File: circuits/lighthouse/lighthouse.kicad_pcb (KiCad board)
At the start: 2 copper layers, 83 x 80 mm, 96 parts, among them IC1 SX1308, J1 USB_C_Receptacle_USB2.0_14P, J2 Conn_01x03_Socket, Q1 S9013, Q2 FS8205A, Q3 2N7002K, Q4 SS8050, Q5 SS8050, U1 R300, U10 CP2102-GMR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

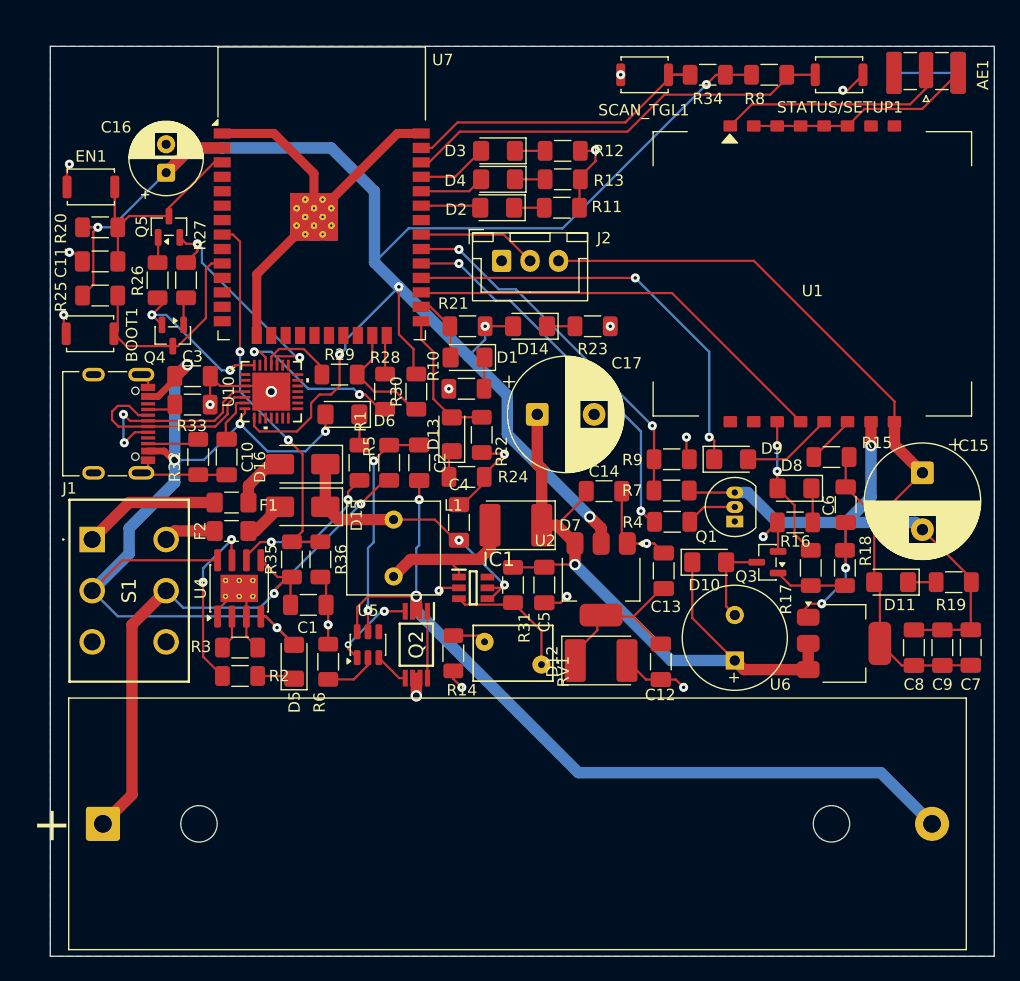
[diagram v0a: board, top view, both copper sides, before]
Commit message: Removed silkscreen numbering
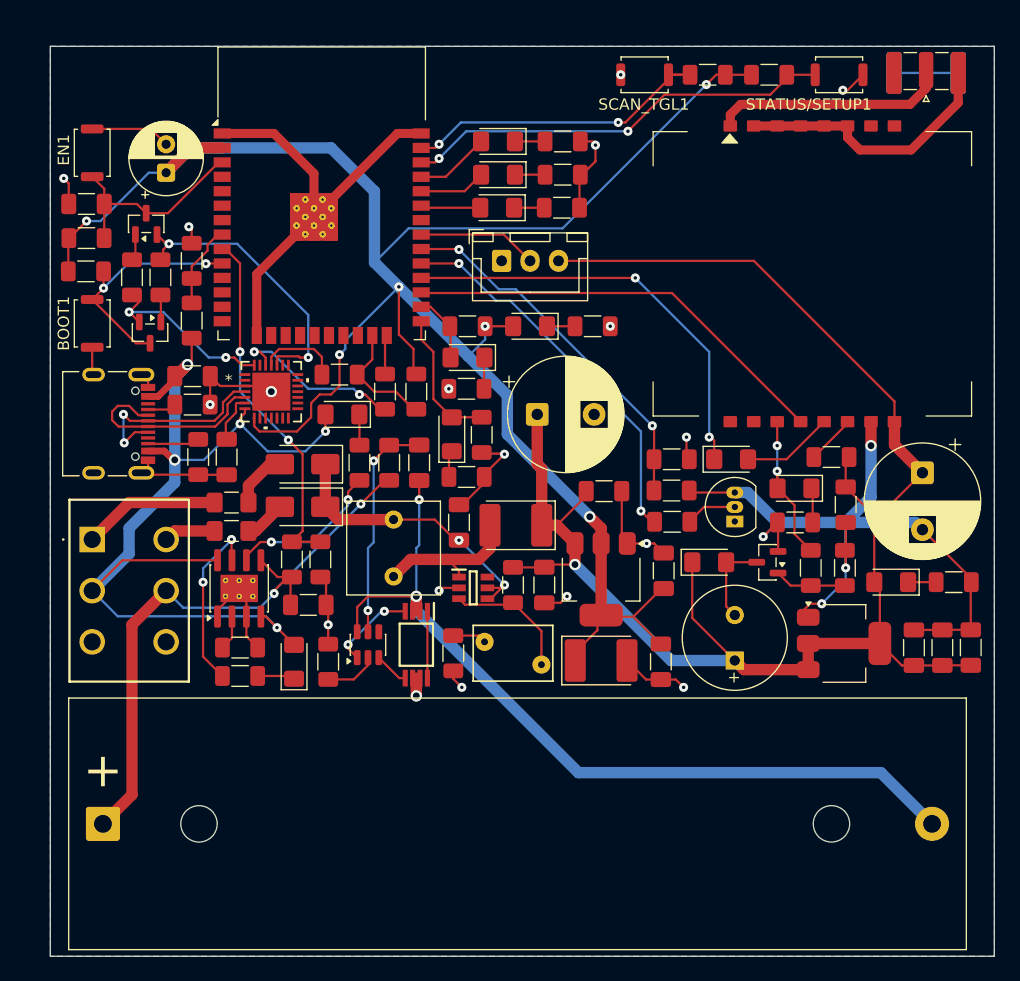
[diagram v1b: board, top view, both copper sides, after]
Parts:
- added R37: 47k, Resistor_SMD:R_1206_3216Metric_Pad1.30x1.75mm_HandSolder, F.Cu at (44.5, 73.2)
- added R38: 100k, Resistor_SMD:R_1206_3216Metric_Pad1.30x1.75mm_HandSolder, F.Cu at (44.5, 78.5)
- moved C11 5.19 mm to (35.2, 68.2)
- moved EN1 3.00 mm to (35.8, 63.8), turned to -90 degrees
- moved R25 2.46 mm to (35.2, 74.2)
- moved R26 2.26 mm to (39.2, 74.7)
- moved R27 2.26 mm to (41.8, 74.7)
- moved Q4 2.02 mm to (40.8, 79.6)
- moved Q5 2.02 mm to (40.5, 70.0)
- moved R20 1.53 mm to (35.2, 71.2)
- moved BOOT1 0.93 mm to (35.8, 78.8), turned to 90 degrees
- moved D3 0.83 mm to (71.4, 62.8)
- moved R12 0.83 mm to (77.1, 62.8)
- moved D4 0.41 mm to (71.4, 65.7)
- moved R13 0.41 mm to (77.1, 65.7)
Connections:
- U7 pad 8: ADS_BAT -> USB_SENSE
- U7 pad 9: unconnected-(U7-IO33-Pad9) -> ADS_BAT
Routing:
- net GND: track 123.4 -> 131.6 mm, vias 19 -> 18
- net USB_SENSE: track 0.00 -> 7.35 mm
- net +5V: track 135.6 -> 141.9 mm
- net MP24: track 20.5 -> 25.1 mm
- net +3.3V: track 171.2 -> 175.5 mm
- net Net-(AE1-Shield): track 25.8 -> 29.7 mm
- net ESP25: track 19.1 -> 21.0 mm, vias 0 -> 2
- net MP28: track 13.9 -> 15.6 mm
- net ADS_BAT: track 33.6 -> 32.0 mm
- net Net-(U7-IO22): track 37.4 -> 38.2 mm, vias 0 -> 2
- net Net-(Q4-B): track 3.12 -> 2.46 mm
- net Net-(AE1-A): track 20.2 -> 20.8 mm
- net Net-(U10-RXD): track 6.79 -> 7.32 mm
- net Net-(U7-IO23): vias 0 -> 2
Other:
- board text removed: "R9"

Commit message: Safekeeping
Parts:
- removed R31: 1k, Resistor_SMD:R_1206_3216Metric_Pad1.30x1.75mm_HandSolder
- removed S1: SLW-1678105-6A-N-D, SLW-1678105-6A-N-D:SLW16781056AND
- added SW1: SW_Push_DPDT, Connector_JST:JST_XH_B4B-XH-A_1x04_P2.50mm_Vertical, F.Cu at (38.2, 105.5)
- D1, D2, D3, D4: footprint LED_SMD:LED_1206_3216Metric_Pad1.42x1.75mm_HandSolder -> LED_THT:LED_D3.0mm
- Q1: value S9013 -> BC337
- Q4, Q5: value SS8050 -> BC817-40
- R14: value 200 -> 220
- R4: value 240 -> 150
- R7: value 10k -> 100k
- R9: value 20k -> 47k
- RV1: value 8k4 -> W103; footprint Varistor:RV_Disc_D7mm_W4.9mm_P5mm -> 3296W-1-103LF:3296W1503LF
- moved R14 8.33 mm to (73.0, 101.5), turned to 90 degrees
- moved D2 7.84 mm to (78.8, 66.0), turned to -90 degrees
- moved R12 7.34 mm to (69.8, 63.2)
- moved R11 5.98 mm to (79.8, 63.2)
- moved D3 3.64 mm to (69.8, 66.0), turned to -90 degrees
- moved R13 3.39 mm to (74.8, 63.2)
- moved D4 2.83 mm to (74.2, 66.0), turned to -90 degrees
- moved J1 2.07 mm to (34.9, 87.6)
- moved RV1 2.02 mm to (73.5, 107.8), turned to 0 degrees
- moved D1 1.52 mm to (70.3, 81.8)
- moved Q2 1.25 mm to (63.0, 107.0)
- moved R6 1.00 mm to (55.5, 108.5)
- moved R2 0.84 mm to (47.9, 110.0)
- moved R3 0.84 mm to (47.9, 107.5)
- moved U4 0.84 mm to (47.9, 102.3)
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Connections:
- RV1 pad 1: Net-(IC1-FB) -> Net-(R14-Pad1)
- RV1 pad 2: Net-(R14-Pad1) -> Net-(IC1-FB)
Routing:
- net +3.3V: track 175.5 -> 139.8 mm
- net +5V: track 141.9 -> 154.3 mm
- net WIFI_STS: track 5.52 -> 17.2 mm, vias 0 -> 1
- net GND: track 131.6 -> 141.3 mm
- net /Charger/VIN: track 86.4 -> 80.0 mm, vias 5 -> 7
- net Net-(SW1-A): track 4.57 -> 10.8 mm
- net ACTIVE_SCAN: track 6.56 -> 12.6 mm, vias 0 -> 1
- net Net-(IC1-FB): track 11.5 -> 6.03 mm
- net /Charger/-BAT: track 74.4 -> 77.1 mm
- net /Charger/CC2: track 4.41 -> 6.51 mm
- net /Charger/CC1: track 2.53 -> 4.60 mm
- net Net-(U10-D-): track 18.0 -> 20.1 mm
- net Net-(U10-D+): track 17.5 -> 19.6 mm
- net Net-(R14-Pad1): track 2.98 -> 4.91 mm
- net Net-(F1-Pad1): track 12.1 -> 10.8 mm
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
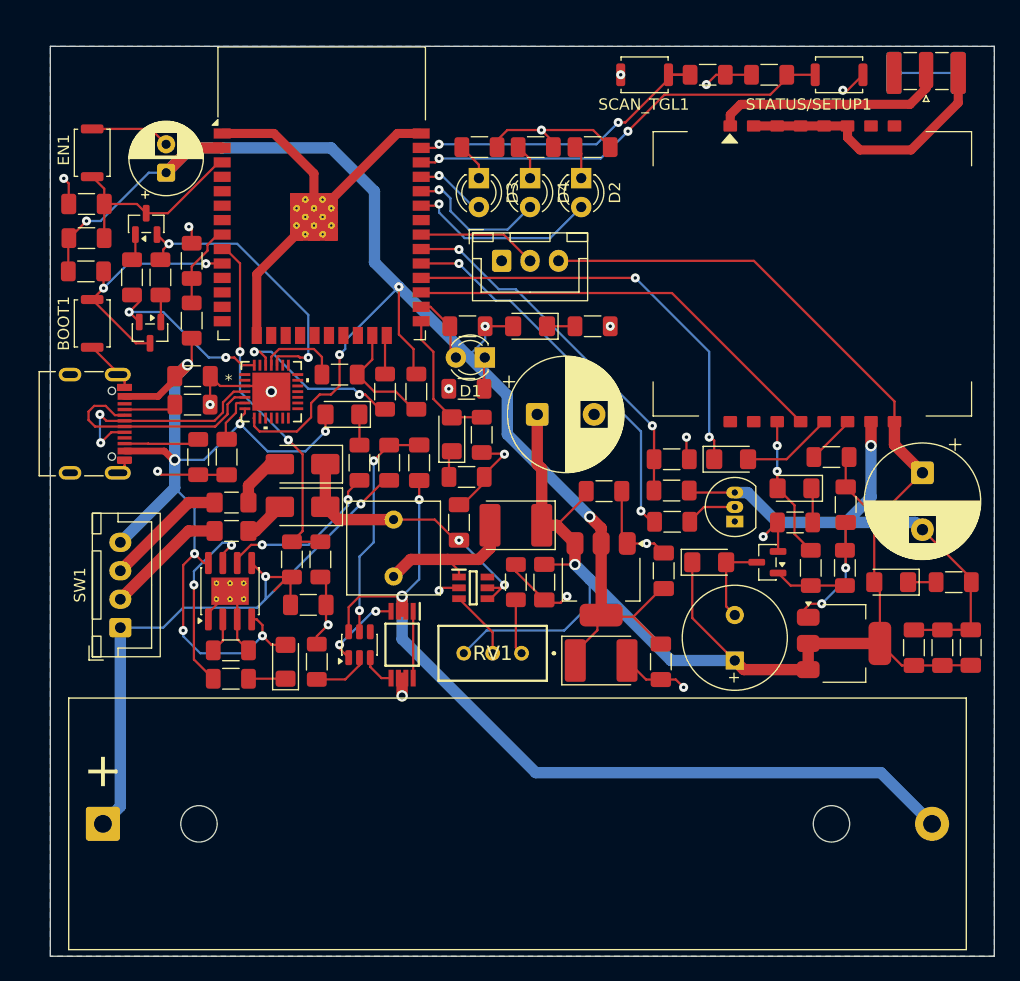
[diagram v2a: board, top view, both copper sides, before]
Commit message: Finalized the board (experiment pending)
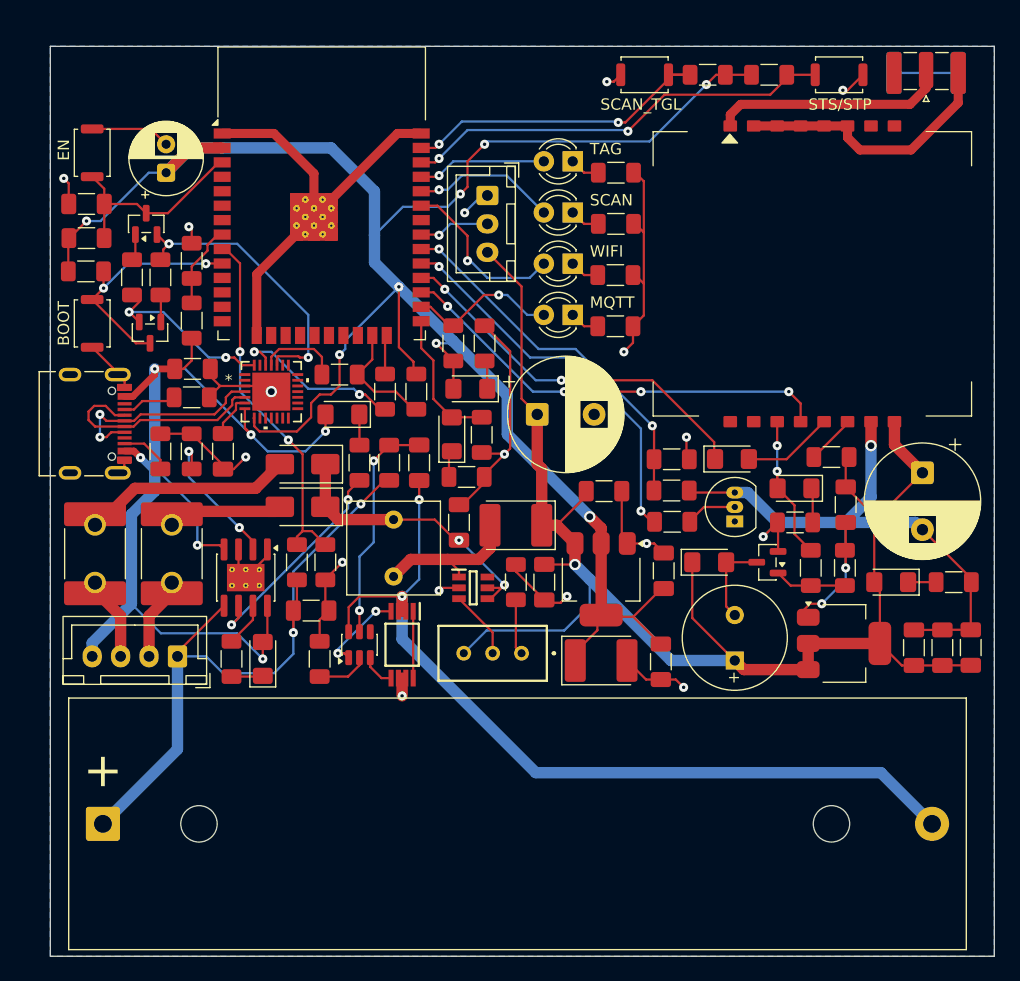
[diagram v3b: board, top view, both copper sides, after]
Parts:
- D9: value LED -> D
- F1, F2: footprint Fuse:Fuse_1206_3216Metric_Pad1.42x1.75mm_HandSolder -> Fuse:Fuse_2920_7451Metric_Pad2.10x5.45mm_HandSolder
- moved R3 17.8 mm to (44.5, 90.0), turned to 90 degrees
- moved R10 14.2 mm to (81.8, 79.0), turned to 0 degrees
- moved F1 12.8 mm to (36.0, 99.0), turned to 90 degrees
- moved R12 12.2 mm to (81.8, 65.5)
- moved R11 11.4 mm to (81.8, 74.5)
- moved R13 9.76 mm to (81.8, 70.0)
- moved R23 9.62 mm to (70.2, 80.5), turned to -90 degrees
- moved D1 8.59 mm to (78.0, 78.0)
- moved D3 8.38 mm to (78.0, 64.5), turned to 180 degrees
- moved D14 7.60 mm to (69.0, 84.5)
- moved D2 7.56 mm to (78.0, 73.5), turned to 180 degrees
- moved J2 5.88 mm to (70.5, 67.5), turned to -90 degrees
- moved SW1 5.62 mm to (43.2, 108.0), turned to 180 degrees
- moved F2 5.62 mm to (42.8, 99.0), turned to 90 degrees
- moved D4 4.81 mm to (78.0, 69.0), turned to 180 degrees
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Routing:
- net +3.3V: track 139.8 -> 176.3 mm, vias 6 -> 8
- net GND: track 141.3 -> 164.5 mm, vias 18 -> 16
- net +5V: track 154.3 -> 133.9 mm
- net /Charger/VIN: track 80.0 -> 93.4 mm, vias 7 -> 6
- net Net-(D16-A): track 5.03 -> 18.0 mm
- net Net-(U4-~{CHRG}): track 16.5 -> 3.91 mm, vias 2 -> 0
- net Net-(U4-PROG): track 3.07 -> 12.5 mm, vias 0 -> 2
- net MQTT_STS: track 6.00 -> 13.1 mm, vias 0 -> 1
- net Net-(D15-A): track 3.64 -> 9.42 mm
- net SCAN_DETECTED: track 6.26 -> 11.6 mm
- net Net-(U4-~{STDBY}): track 14.7 -> 19.3 mm
- net PIR: track 10.7 -> 6.45 mm, vias 0 -> 1
- net TX: track 37.7 -> 33.6 mm
- net Net-(SW1-A): track 10.8 -> 6.73 mm
- net Net-(F1-Pad1): track 10.8 -> 6.73 mm
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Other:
- board text added: "BOOT"
- board text added: "EN"
- board text added: "MQTT"
- board text added: "SCAN"
- board text added: "SCAN_TGL"
- board text added: "STS/STP"
- board text added: "TAG"
- board text added: "WIFI"

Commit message: You would have haaaaaaated yourself were you to order the pcb before this commit. Some pins cannot be exchanged, you even labeled them so. DUm Dum
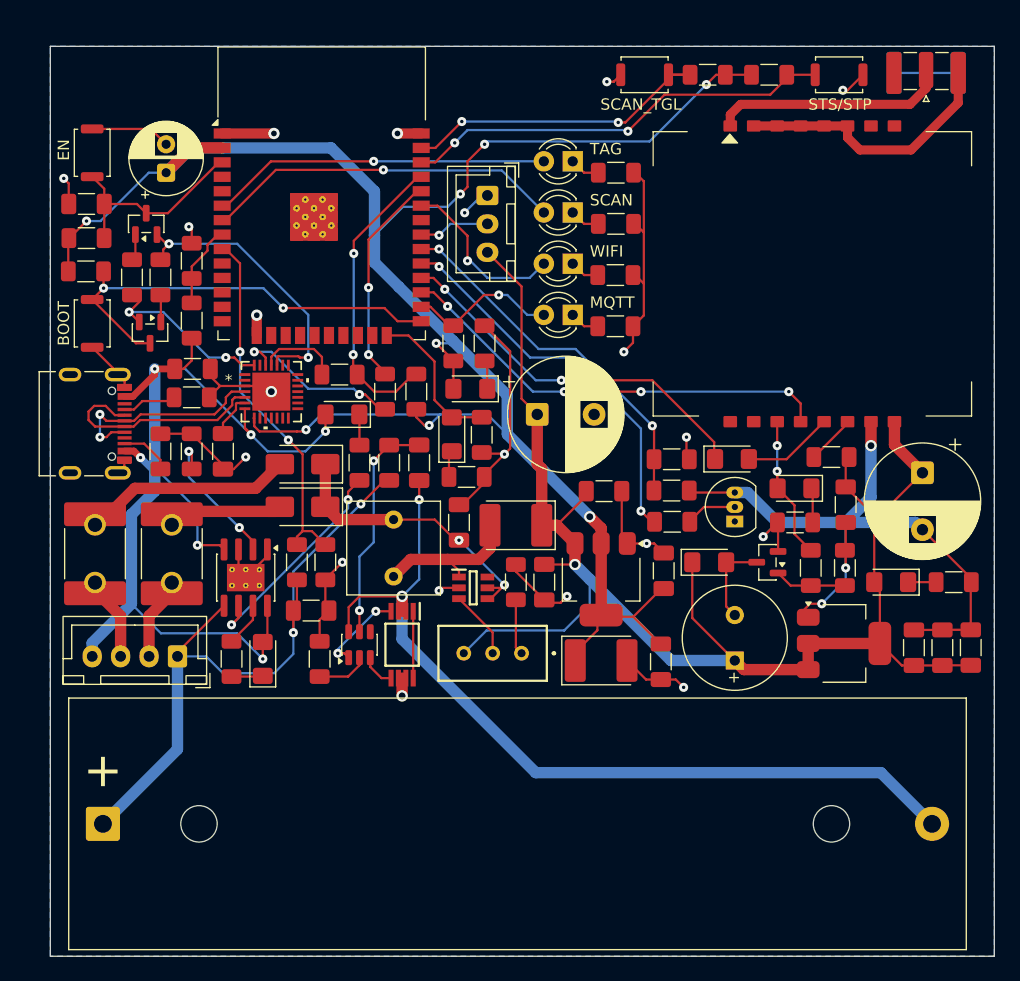
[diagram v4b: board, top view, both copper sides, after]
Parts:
- turned R30 to 90 degrees
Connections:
- R28 pad 1: ESP35 -> ESP34
- R29 pad 1: ESP34 -> ESP35
- R30 pad 2: ESP34 -> ESP35
- U7 pad 10: ESP25 -> unconnected-(U7-IO25-Pad10)
- U7 pad 23: ESP34 -> unconnected-(U7-IO15-Pad23)
- U7 pad 24: ESP35 -> ESP24
- U7 pad 25: ESP24 -> ESP25
- U7 pad 34: ACTIVE_SCAN -> ESP34
- U7 pad 35: SCAN_DETECTED -> ESP35
- U7 pad 6: unconnected-(U7-IO34-Pad6) -> SCAN_DETECTED
- U7 pad 7: unconnected-(U7-IO35-Pad7) -> ACTIVE_SCAN
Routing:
- net GND: track 164.5 -> 134.6 mm, vias 16 -> 19
- net ESP35: track 3.45 -> 27.3 mm, vias 0 -> 2
- net ACTIVE_SCAN: track 12.7 -> 31.7 mm
- net SCAN_DETECTED: track 11.6 -> 29.9 mm
- net ESP25: track 21.0 -> 38.6 mm
- net ESP34: track 10.2 -> 18.8 mm, vias 0 -> 2
- net +3.3V: track 176.3 -> 174.5 mm
- net ESP24: track 12.3 -> 13.7 mm
